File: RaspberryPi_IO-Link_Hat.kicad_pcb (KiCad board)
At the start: 2 copper layers, 65 x 56 mm, 50 parts, among them J1 Jack-DC, J2 Raspberry_Pi_2_3, J3 Conn_01x03_Male, J4 Conn_01x03_Male, J5 Conn_01x03_Male, J6 Conn_01x03_Male, Q1 Q_PMOS_GSD, Q2 Q_NMOS_GSD, Q3 Q_NMOS_GSD, Q4 FQT7N10LTF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

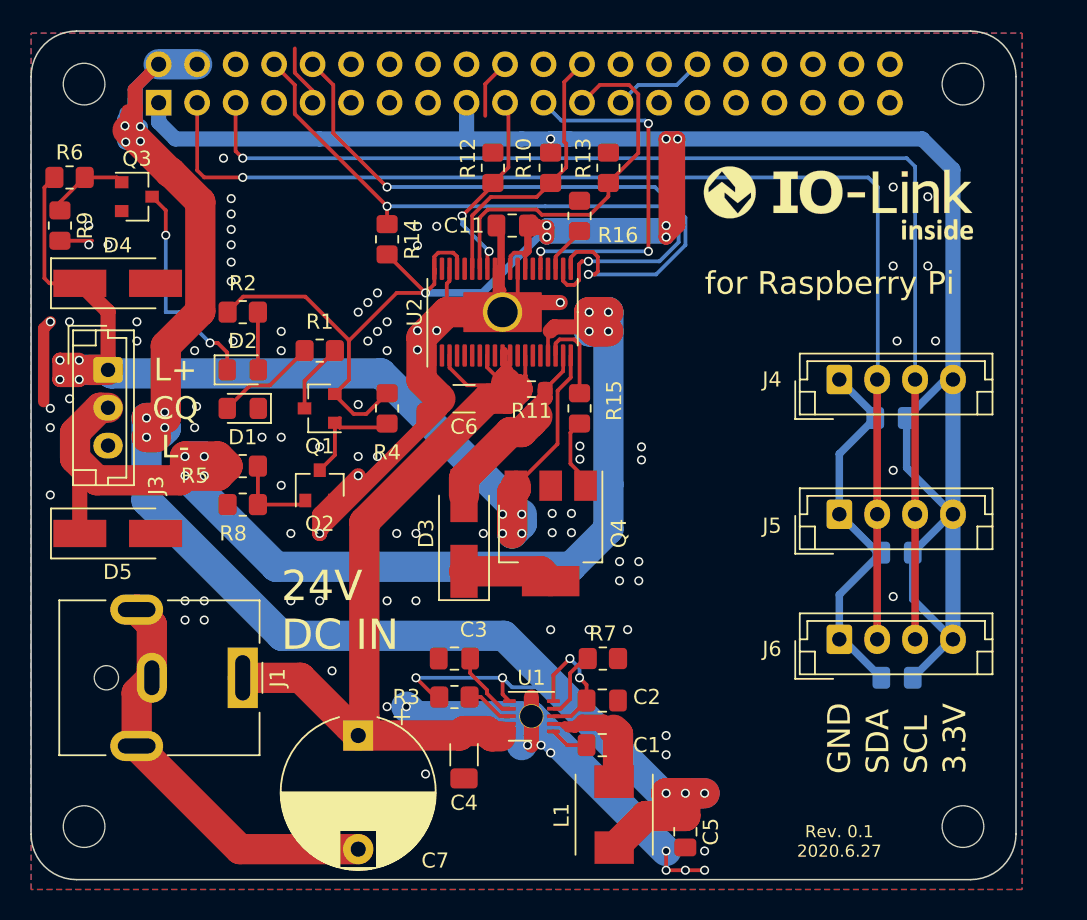
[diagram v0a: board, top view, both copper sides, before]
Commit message: fix: KiCad 5.99 に移行
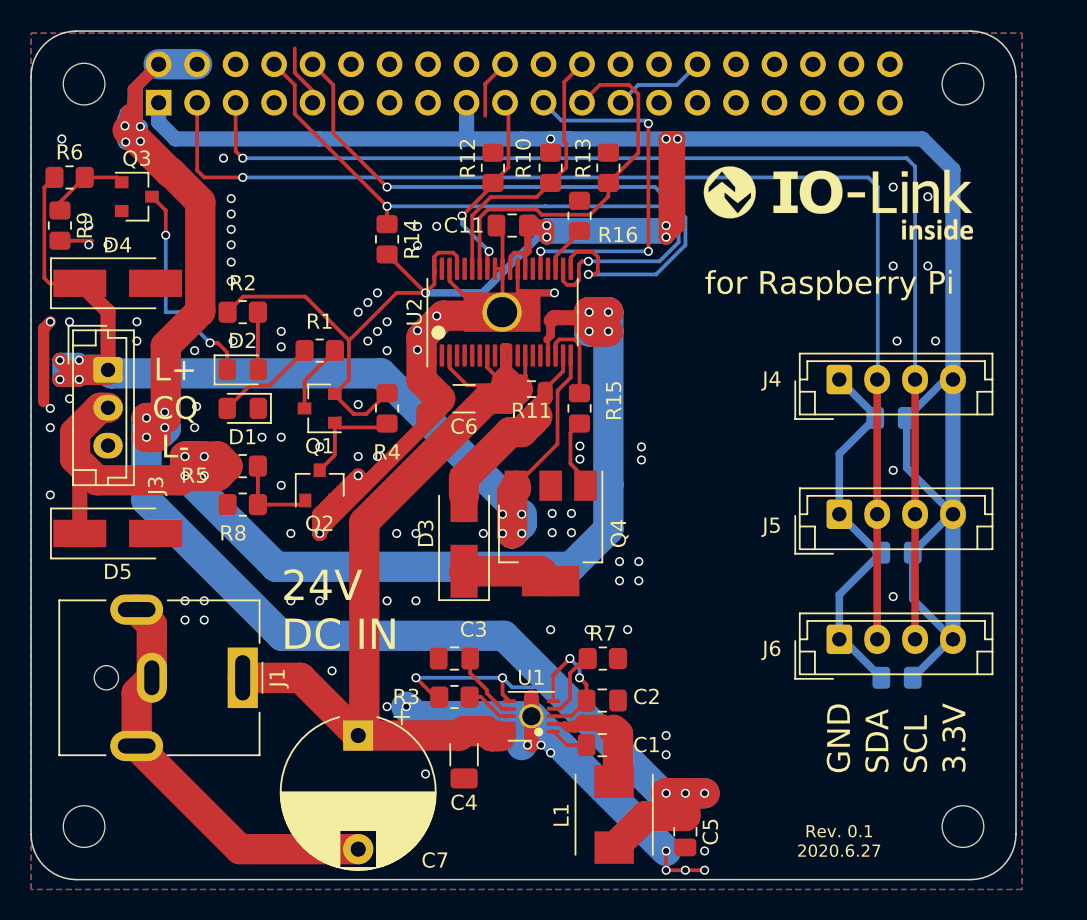
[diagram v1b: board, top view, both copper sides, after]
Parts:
- renumbered G*** to G0
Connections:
- J2 pad 11: Net-(J2-Pad11) -> unconnected-(J2-Pad11)
- J2 pad 12: Net-(J2-Pad12) -> unconnected-(J2-Pad12)
- J2 pad 13: Net-(J2-Pad13) -> unconnected-(J2-Pad13)
- J2 pad 15: Net-(J2-Pad15) -> unconnected-(J2-Pad15)
- J2 pad 16: Net-(J2-Pad16) -> unconnected-(J2-Pad16)
- J2 pad 18: Net-(J2-Pad18) -> unconnected-(J2-Pad18)
- J2 pad 22: Net-(J2-Pad22) -> unconnected-(J2-Pad22)
- J2 pad 26: Net-(J2-Pad26) -> unconnected-(J2-Pad26)
- J2 pad 27: Net-(J2-Pad27) -> unconnected-(J2-Pad27)
- J2 pad 28: Net-(J2-Pad28) -> unconnected-(J2-Pad28)
- J2 pad 29: Net-(J2-Pad29) -> unconnected-(J2-Pad29)
- J2 pad 31: Net-(J2-Pad31) -> unconnected-(J2-Pad31)
- J2 pad 32: Net-(J2-Pad32) -> unconnected-(J2-Pad32)
- J2 pad 33: Net-(J2-Pad33) -> unconnected-(J2-Pad33)
- J2 pad 35: Net-(J2-Pad35) -> unconnected-(J2-Pad35)
- J2 pad 36: Net-(J2-Pad36) -> unconnected-(J2-Pad36)
- J2 pad 37: Net-(J2-Pad37) -> unconnected-(J2-Pad37)
- J2 pad 38: Net-(J2-Pad38) -> unconnected-(J2-Pad38)
- J2 pad 40: Net-(J2-Pad40) -> unconnected-(J2-Pad40)
- J2 pad 7: Net-(J2-Pad7) -> unconnected-(J2-Pad7)
- U2 pad 12: Net-(U2-Pad12) -> unconnected-(U2-Pad12)
- U2 pad 14: Net-(U2-Pad14) -> unconnected-(U2-Pad14)
- U2 pad 15: Net-(U2-Pad15) -> unconnected-(U2-Pad15)
- U2 pad 2: Net-(U2-Pad2) -> unconnected-(U2-Pad2)
- U2 pad 23: Net-(U2-Pad23) -> unconnected-(U2-Pad23)
- U2 pad 25: Net-(U2-Pad25) -> unconnected-(U2-Pad25)
- U2 pad 34: Net-(U2-Pad34) -> unconnected-(U2-Pad34)
- U2 pad 37: Net-(U2-Pad37) -> unconnected-(U2-Pad37)
- U2 pad 4: Net-(U2-Pad4) -> unconnected-(U2-Pad4)
- U2 pad 5: Net-(U2-Pad5) -> unconnected-(U2-Pad5)
- U2 pad 6: Net-(U2-Pad6) -> unconnected-(U2-Pad6)
- U2 pad 7: Net-(U2-Pad7) -> unconnected-(U2-Pad7)
- U2 pad 9: Net-(U2-Pad9) -> unconnected-(U2-Pad9)
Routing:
- net GND: track 157.5 -> 155.3 mm, vias 96 -> 97
- net CQ1: track 89.9 -> 91.9 mm
- net +24V: track 65.7 -> 67.4 mm
- net L+1: track 71.8 -> 73.0 mm
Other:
- net class Default removed

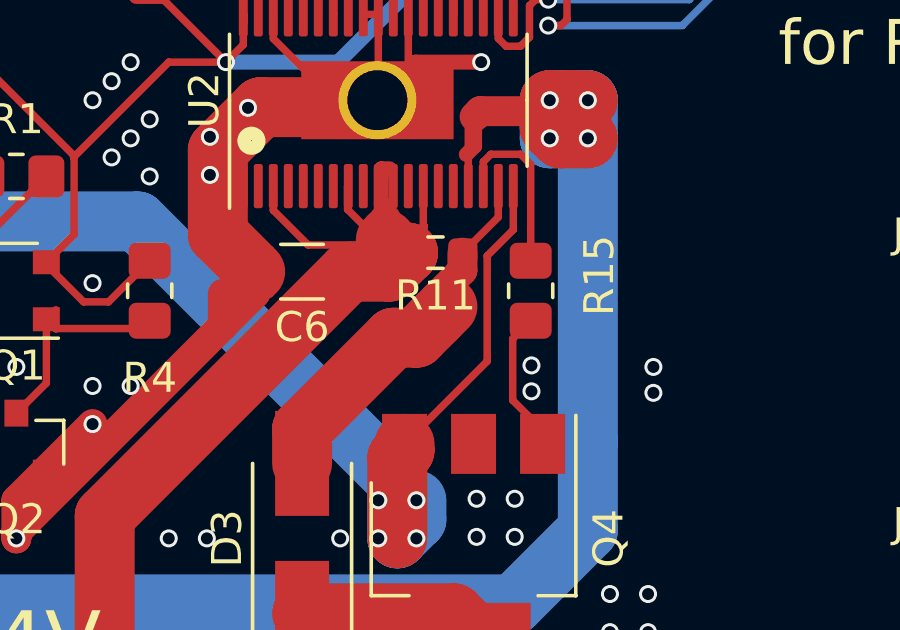
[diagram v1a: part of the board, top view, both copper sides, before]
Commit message: fix: ライブラリの参照がおかしくなっていた問題を修正
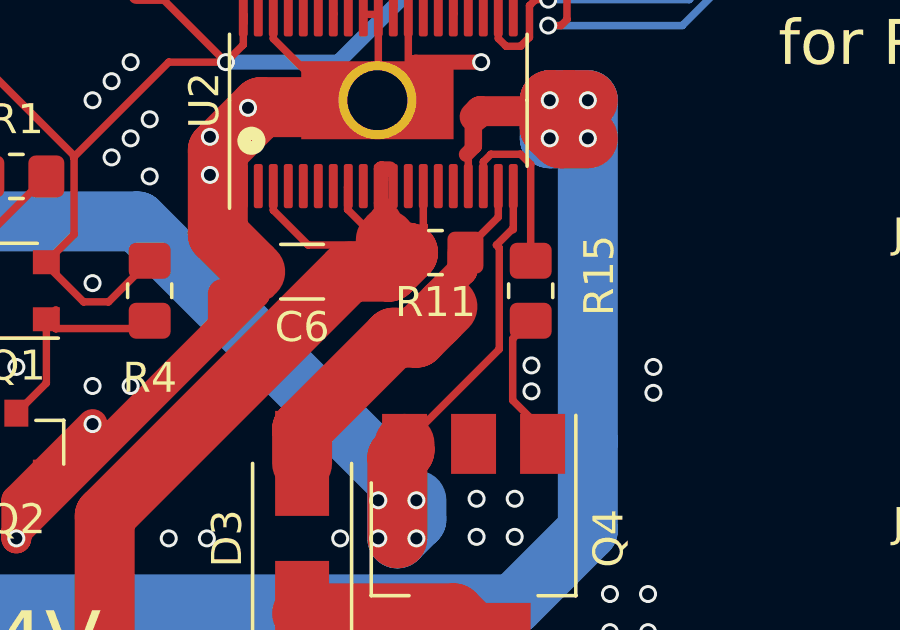
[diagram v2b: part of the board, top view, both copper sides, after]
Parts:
- removed the ? at (79.3, 86.0)
- added ?: , Local:RPi_Hat_Mounting_Hole_Small, F.Cu at (79.3, 86.0)
- R11: footprint Resistor_SMD:R_0603_1608Metric_Pad0.98x0.95mm_HandSolder -> Resistor_SMD:R_0805_2012Metric_Pad1.20x1.40mm_HandSolder
